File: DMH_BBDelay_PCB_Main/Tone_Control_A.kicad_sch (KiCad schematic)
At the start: 11 parts, among them U17 TL072

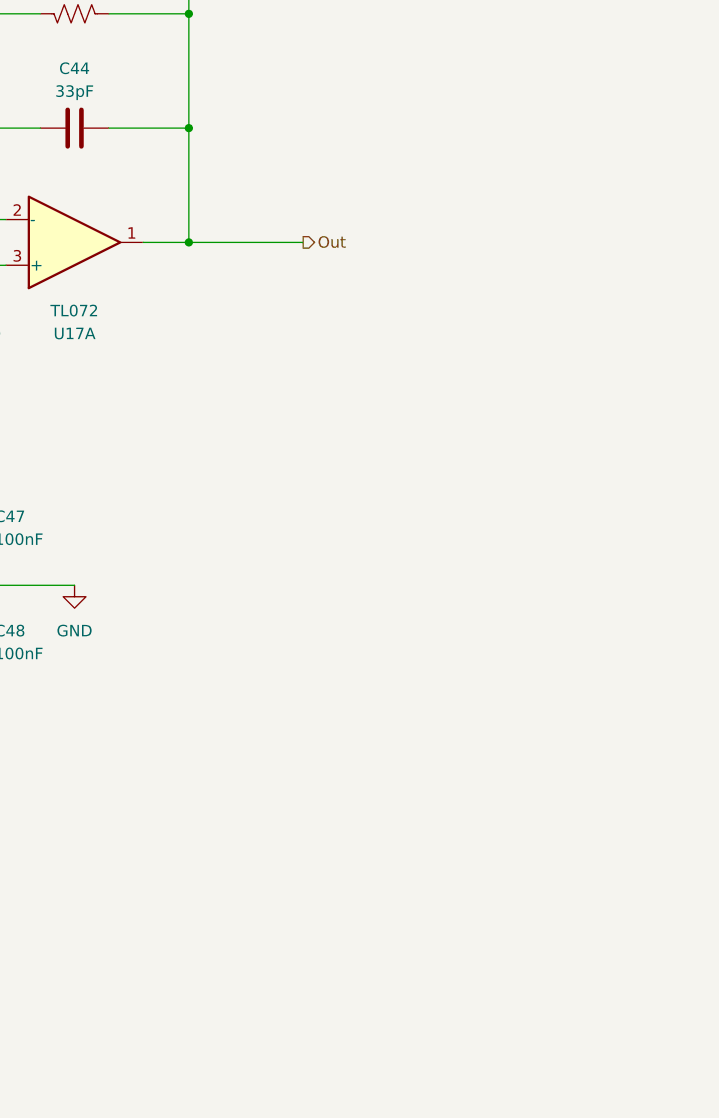
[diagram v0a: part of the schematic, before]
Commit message: Removed compander and adjusted feedback
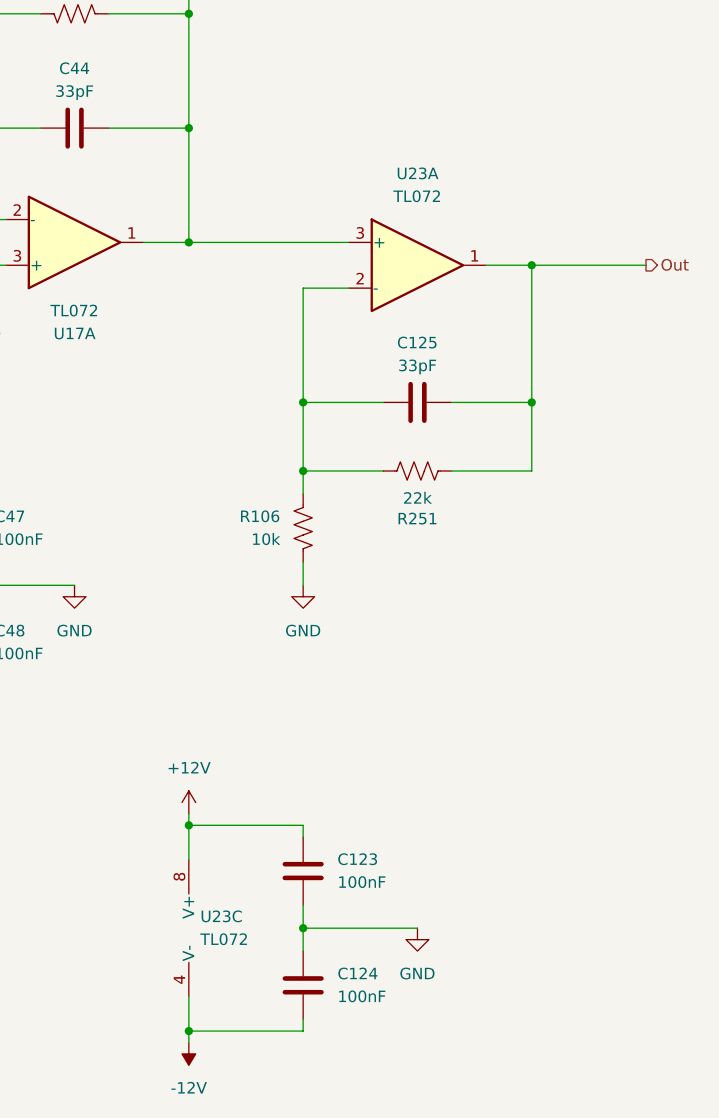
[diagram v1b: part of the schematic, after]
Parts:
- added C123, C124: 100nF, Capacitor_THT:C_Disc_D4.3mm_W1.9mm_P5.00mm, symbol Device:C
- added C125: 33pF, Capacitor_THT:C_Disc_D3.0mm_W2.0mm_P2.50mm, symbol Device:C
- added R106: 10k, Resistor_THT:R_Axial_DIN0207_L6.3mm_D2.5mm_P7.62mm_Horizontal, symbol Device:R_US
- added R251: 22k, Resistor_THT:R_Axial_DIN0207_L6.3mm_D2.5mm_P7.62mm_Horizontal, symbol Device:R_US
- added U23: TL072, Package_DIP:DIP-8_W7.62mm_Socket, symbol Amplifier_Operational:TL072
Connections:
- net +12V: now also C123.1, U23.8 (V+)
- net -12V: now also C124.2, U23.4 (V-)
- net GND: now also C123.2, C124.1, R106.1
- net Out: now also C125.2, R251.2, U23.1; no longer C44.2, R162.2, R163.2, U17.1
- new net: C44.2, R162.2, R163.2, U17.1, U23.3 (+)
- new net: C125.1, R106.2, R251.1, U23.2 (-)

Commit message: Synced channel A and B schematics
... and applied several minor improvements and optimizations.
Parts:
- removed C123, C124: 100nF, Capacitor_THT:C_Disc_D4.3mm_W1.9mm_P5.00mm, symbol Device:C
- removed U17, U23: TL072, Package_DIP:DIP-8_W7.62mm_Socket, symbol Amplifier_Operational:TL072
- added U17: TL074, Package_DIP:DIP-14_W7.62mm_Socket, symbol Amplifier_Operational:TL074
- R251: value 22k -> 20k
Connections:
- net +12V: now also U17.4 (V+)
- net -12V: now also U17.11 (V-)
- net GND: now also U17.3 (+)
- net Out: now also U17.7
- net at C44.2, R162.2, R163.2: now also U17.1, U17.5 (+)
- net at C44.1, RV11.2: now also U17.2 (-)
- net at C125.1, R106.2, R251.1: now also U17.6 (-)

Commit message: Validated gains in breadboard
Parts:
- R251: value 20k -> 22k
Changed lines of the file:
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@@
 			)
 		)
-		(property "Value" "20k"
+		(property "Value" "22k"
 			(at 139.7 104.648 90)
 			(show_name no)

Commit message: Qualified channel A on breadboard
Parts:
- R106: value 10k -> 14k
- R251: value 22k -> 56k
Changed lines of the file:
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@@
 			)
 		)
-		(property "Value" "10k"
+		(property "Value" "14k"
 			(at 124.46 109.2199 0)
 			(show_name no)
@@
 			)
 		)
-		(property "Value" "22k"
+		(property "Value" "56k"
 			(at 139.7 104.648 90)
 			(show_name no)
